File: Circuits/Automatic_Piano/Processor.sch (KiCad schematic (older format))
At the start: 1 part

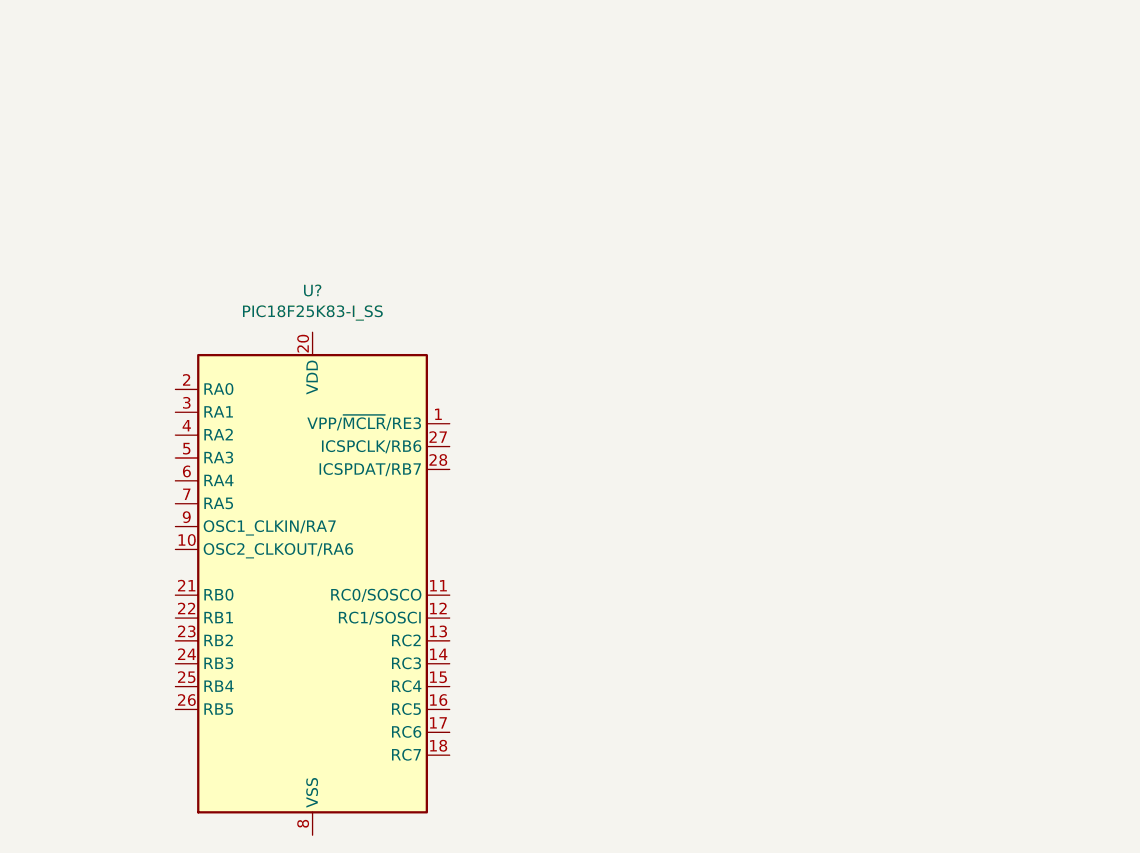
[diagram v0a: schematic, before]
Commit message: Main Piano MIDI receiver completed. Might want indicator LEDS and more peripherals.
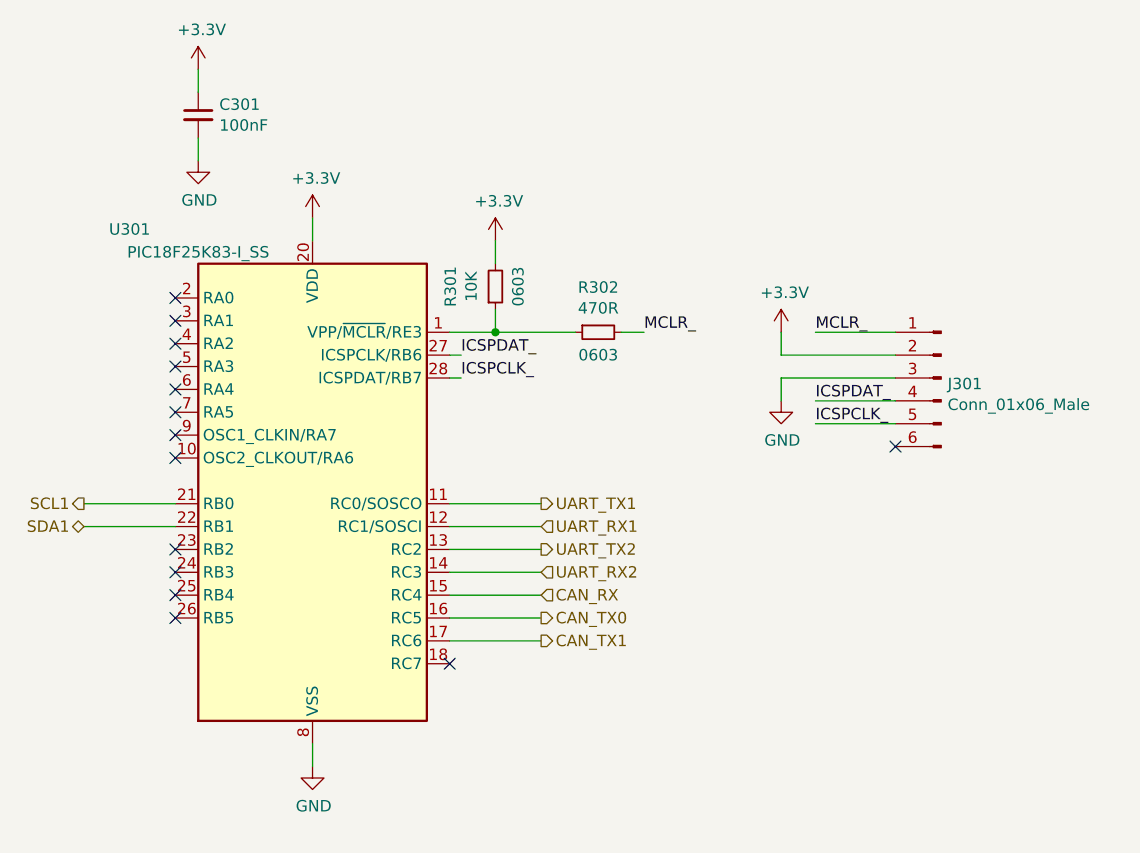
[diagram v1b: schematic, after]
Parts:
- added C301: 100nF, symbol Device:C_Small
- added J301: Conn_01x06_Male, symbol Connector:Conn_01x06_Male
- added R301: 10K, Resistor_SMD:R_0603_1608Metric, symbol Device:R_Small
- added R302: 470R, Resistor_SMD:R_0603_1608Metric, symbol Device:R_Small
- gave numbers to parts that had none: 1
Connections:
- net at U301.1 (VPP/~MCLR~/RE3): now also R301.1, R302.1
- net UART_TX1: now reaches U301.11 (RC0/SOSCO)
- net UART_RX1: now reaches U301.12 (RC1/SOSCI)
- net UART_TX2: now reaches U301.13 (RC2)
- net UART_RX2: now reaches U301.14 (RC3)
- net CAN_RX: now reaches U301.15 (RC4)
- net CAN_TX0: now reaches U301.16 (RC5)
- net CAN_TX1: now reaches U301.17 (RC6)
- net GND: now reaches U301.19 (VSS), U301.8 (VSS)
- net GND: now also C301.2, J301.3 (Pin_3)
- net +3V3: now reaches U301.20 (VDD)
- net +3V3: now also C301.1, J301.2 (Pin_2), R301.2
- net SCL1: now reaches U301.21 (RB0)
- net SDA1: now reaches U301.22 (RB1)
- net ICSPDAT_: now reaches U301.27 (ICSPCLK/RB6)
- net ICSPDAT_: now also J301.4 (Pin_4)
- net ICSPCLK_: now reaches U301.28 (ICSPDAT/RB7)
- net ICSPCLK_: now also J301.5 (Pin_5)
- new net MCLR_: J301.1 (Pin_1), R302.2
- no-connect marks 0 -> 14
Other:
- moved on the sheet: U301
